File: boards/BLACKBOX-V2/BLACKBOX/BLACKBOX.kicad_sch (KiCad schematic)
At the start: 24 parts, among them J1 Micro_SD_Card, J2 Conn_01x07_Female, J3 Conn_01x02_Female, U1 Adafruit-BNO085, U2 KX122-1042, U3 MS5611-01BA

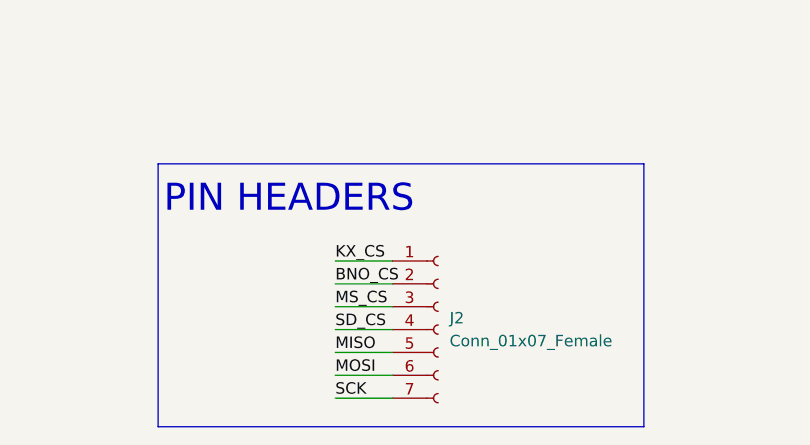
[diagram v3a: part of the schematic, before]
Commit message: Updated pcb and schematic to have 8pin headers
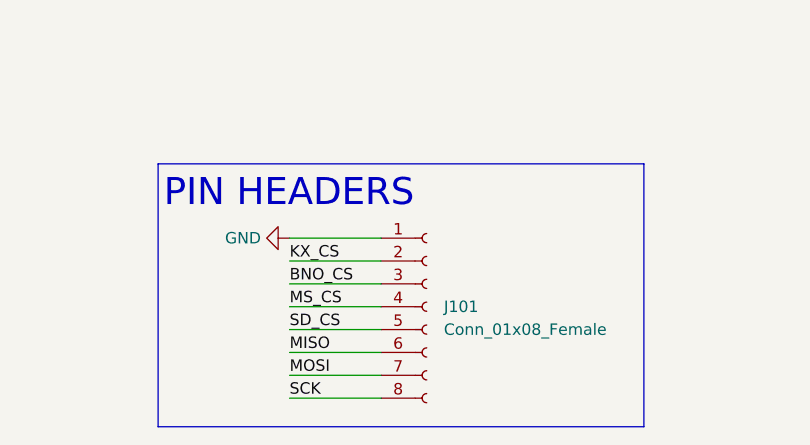
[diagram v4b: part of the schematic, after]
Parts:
- removed J2: Conn_01x07_Female, Connector_PinHeader_2.54mm:PinHeader_1x07_P2.54mm_Vertical, symbol Connector:Conn_01x07_Female
- added J101: Conn_01x08_Female, Connector_PinHeader_2.54mm:PinHeader_1x08_P2.54mm_Vertical, symbol Connector:Conn_01x08_Female
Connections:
- net BNO_CS: now also J101.3 (Pin_3)
- net GND: now also J101.1 (Pin_1)
- net KX_CS: now also J101.2 (Pin_2)
- net MISO: now also J101.6 (Pin_6)
- net MOSI: now also J101.7 (Pin_7)
- net MS_CS: now also J101.4 (Pin_4)
- net SCK: now also J101.8 (Pin_8)
- net SD_CS: now also J101.5 (Pin_5)
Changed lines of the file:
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@@
     (stroke (width 0) (type default) (color 0 0 0 0))
   )
-  (wire (pts (xy 132.715 186.69) (xy 139.065 186.69))
+  (wire (pts (xy 127.635 186.69) (xy 137.795 186.69))
     (stroke (width 0) (type default) (color 0 0 0 0))
   )
@@
     (stroke (width 0) (type default) (color 0 0 0 0))
   )
-  (wire (pts (xy 132.715 179.07) (xy 139.065 179.07))
+  (wire (pts (xy 127.635 179.07) (xy 137.795 179.07))
     (stroke (width 0) (type default) (color 0 0 0 0))
   )
@@
     (stroke (width 0) (type default) (color 0 0 0 0))
   )
-  (wire (pts (xy 132.715 173.99) (xy 139.065 173.99))
-    (stroke (width 0) (type default) (color 0 0 0 0))
-  )
-  (wire (pts (xy 132.715 184.15) (xy 139.065 184.15))
+  (wire (pts (xy 127.635 173.99) (xy 137.795 173.99))
+    (stroke (width 0) (type default) (color 0 0 0 0))
+  )
+  (wire (pts (xy 127.635 184.15) (xy 137.795 184.15))
     (stroke (width 0) (type default) (color 0 0 0 0))
   )
@@
     (stroke (width 0) (type default) (color 0 0 0 0))
   )
-  (wire (pts (xy 132.715 181.61) (xy 139.065 181.61))
+  (wire (pts (xy 127.635 181.61) (xy 137.795 181.61))
     (stroke (width 0) (type default) (color 0 0 0 0))
   )
@@
     (stroke (width 0) (type default) (color 0 0 0 0))
   )
+  (wire (pts (xy 127.635 168.91) (xy 137.795 168.91))
+    (stroke (width 0) (type default) (color 0 0 0 0))
+  )
   (wire (pts (xy 158.75 36.83) (xy 158.75 38.1))
     (stroke (width 0) (type default) (color 0 0 0 0))
@@
     (stroke (width 0) (type default) (color 0 0 0 0))
   )
-  (wire (pts (xy 132.715 176.53) (xy 139.065 176.53))
+  (wire (pts (xy 127.635 176.53) (xy 137.795 176.53))
     (stroke (width 0) (type default) (color 0 0 0 0))
   )
@@
     (stroke (width 0) (type default) (color 0 0 0 0))
   )
-  (wire (pts (xy 132.715 171.45) (xy 139.065 171.45))
+  (wire (pts (xy 127.635 171.45) (xy 137.795 171.45))
     (stroke (width 0) (type default) (color 0 0 0 0))
   )
@@
     (effects (font (size 3.2004 3.2004)) (justify left bottom))
   )
-  (text "PIN HEADERS" (at 113.665 166.37 0)
+  (text "PIN HEADERS" (at 113.665 165.735 0)
     (effects (font (size 3 3)) (justify left bottom))
   )
@@
     (effects (font (size 1.27 1.27)) (justify left bottom))
   )
-  (label "SCK" (at 132.715 186.69 0)
+  (label "SCK" (at 127.635 186.69 0)
     (effects (font (size 1.27 1.27)) (justify left bottom))
   )
@@
     (effects (font (size 1.27 1.27)) (justify left bottom))
   )
-  (label "MISO" (at 132.715 181.61 0)
+  (label "MISO" (at 127.635 181.61 0)
     (effects (font (size 1.27 1.27)) (justify left bottom))
   )
@@
     (effects (font (size 1.27 1.27)) (justify left bottom))
   )
-  (label "MS_CS" (at 132.715 176.53 0)
+  (label "MS_CS" (at 127.635 176.53 0)
     (effects (font (size 1.27 1.27)) (justify left bottom))
   )
@@
     (effects (font (size 1.27 1.27)) (justify left bottom))
   )
-  (label "KX_CS" (at 132.715 171.45 0)
+  (label "KX_CS" (at 127.635 171.45 0)
     (effects (font (size 1.27 1.27)) (justify left bottom))
   )
@@
     (effects (font (size 1.27 1.27)) (justify left bottom))
   )
-  (label "MOSI" (at 132.715 184.15 0)
+  (label "MOSI" (at 127.635 184.15 0)
     (effects (font (size 1.27 1.27)) (justify left bottom))
   )
@@
     (effects (font (size 1.27 1.27)) (justify left bottom))
   )
-  (label "SD_CS" (at 132.715 179.07 0)
+  (label "SD_CS" (at 127.635 179.07 0)
     (effects (font (size 1.27 1.27)) (justify left bottom))
   )
@@
     (effects (font (size 1.27 1.27)) (justify left bottom))
   )
-  (label "BNO_CS" (at 132.715 173.99 0)
+  (label "BNO_CS" (at 127.635 173.99 0)
     (effects (font (size 1.27 1.27)) (justify left bottom))
   )
@@
     (pin "2")
   )
-  (symbol (lib_id "Connector:Conn_01x07_Female") (at 144.145 179.07 0) (unit 1)
-    (in_bom yes) (on_board yes) (fields_autoplaced)
-    (property "Reference" "J2" (id 0) (at 145.415 177.7999 0)
-      (effects (font (size 1.27 1.27)) (justify left))
-    )
-    (property "Value" "Conn_01x07_Female" (id 1) (at 145.415 180.3399 0)
-      (effects (font (size 1.27 1.27)) (justify left))
-    )
-    (property "Footprint" "Connector_PinHeader_2.54mm:PinHeader_1x07_P2.54mm_Vertical" (id 2) (at 144.145 179.07 0)
-      (effects (font (size 1.27 1.27)) hide)
-    )
-    (property "Datasheet" "~" (id 3) (at 144.145 179.07 0)
-      (effects (font (size 1.27 1.27)) hide)
-    )
-    (pin "1")
-    (pin "2")
-    (pin "3")
-    (pin "4")
-    (pin "5")
-    (pin "6")
-    (pin "7")
-  )
   (symbol (lib_id "Device:C_Small") (at 78.74 26.035 90) (unit 1)
     (in_bom yes) (on_board yes) (fields_autoplaced)
@@
     (pin "1")
   )
+  (symbol (lib_id "Connector:Conn_01x08_Female") (at 142.875 176.53 0) (unit 1)
+    (in_bom yes) (on_board yes) (fields_autoplaced)
+    (property "Reference" "J101" (id 0) (at 144.78 176.5299 0)
+      (effects (font (size 1.27 1.27)) (justify left))
+    )
+    (property "Value" "Conn_01x08_Female" (id 1) (at 144.78 179.0699 0)
+      (effects (font (size 1.27 1.27)) (justify left))
+    )
+    (property "Footprint" "Connector_PinHeader_2.54mm:PinHeader_1x08_P2.54mm_Vertical" (id 2) (at 142.875 176.53 0)
+      (effects (font (size 1.27 1.27)) hide)
+    )
+    (property "Datasheet" "~" (id 3) (at 142.875 176.53 0)
+      (effects (font (size 1.27 1.27)) hide)
+    )
+    (pin "1")
+    (pin "2")
+    (pin "3")
+    (pin "4")
+    (pin "5")
+    (pin "6")
+    (pin "7")
+    (pin "8")
+  )
+  (symbol (lib_id "power:GND") (at 127.635 168.91 270) (unit 1)
+    (in_bom yes) (on_board yes)
+    (property "Reference" "#PWR0101" (id 0) (at 121.285 168.91 0)
+      (effects (font (size 1.27 1.27)) hide)
+    )
+    (property "Value" "GND" (id 1) (at 124.46 168.9099 90)
+      (effects (font (size 1.27 1.27)) (justify right))
+    )
+    (property "Footprint" "" (id 2) (at 127.635 168.91 0)
+      (effects (font (size 1.27 1.27)) hide)
+    )
+    (property "Datasheet" "" (id 3) (at 127.635 168.91 0)
+      (effects (font (size 1.27 1.27)) hide)
+    )
+    (pin "1")
+  )
   (symbol (lib_id "Device:Jumper_NC_Small") (at 252.222 33.274 0) (unit 1)
     (in_bom yes) (on_board yes)
@@
       (reference "#PWR018") (unit 1) (value "GND") (footprint "")
     )
+    (path "/9a261a05-f51b-41db-af95-8182bda7df0f"
+      (reference "#PWR0101") (unit 1) (value "GND") (footprint "")
+    )
     (path "/04c2f4a0-ab0f-4d7a-91c1-dde2ab8ebf89"
       (reference "A1") (unit 1) (value "Arduino_Nano_v3.x") (footprint "Module:Arduino_Nano")
@@
       (reference "J1") (unit 1) (value "Micro_SD_Card") (footprint "Connector_Card:microSD_HC_Hirose_DM3AT-SF-PEJM5")
     )
-    (path "/28be4453-0358-472e-94e9-5e8d78d2b655"
-      (reference "J2") (unit 1) (value "Conn_01x07_Female") (footprint "Connector_PinHeader_2.54mm:PinHeader_1x07_P2.54mm_Vertical")
-    )
     (path "/eaf8df72-2293-43bc-a95d-5a36de237e99"
       (reference "J3") (unit 1) (value "Conn_01x02_Female") (footprint "Connector_JST:JST_PH_B2B-PH-K_1x02_P2.00mm_Vertical")
     )
+    (path "/8c1aa14f-b92e-48a9-8685-2f98cff5b3f9"
+      (reference "J101") (unit 1) (value "Conn_01x08_Female") (footprint "Connector_PinHeader_2.54mm:PinHeader_1x08_P2.54mm_Vertical")
+    )
     (path "/30afc378-2f36-4761-a0c7-cd6bc7d246e3"

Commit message: Completed power thingy
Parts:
- added J102: Conn_01x02_Female, Connector_JST:JST_PH_B2B-PH-K_1x02_P2.00mm_Vertical, symbol Connector:Conn_01x02_Female
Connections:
- net GND: now also J102.1 (Pin_1); no longer J3.1 (Pin_1)
- new net VBUS: J102.2 (Pin_2), J3.1 (Pin_1)
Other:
- moved on the sheet: J3
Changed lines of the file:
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@@
     (stroke (width 0) (type default) (color 0 0 0 0))
   )
-  (polyline (pts (xy 279.4 96.52) (xy 279.4 72.39))
+  (polyline (pts (xy 279.4 104.775) (xy 279.4 72.39))
     (stroke (width 0) (type default) (color 0 0 0 0))
   )
@@
     (stroke (width 0) (type default) (color 0 0 0 0))
   )
-  (wire (pts (xy 242.57 83.82) (xy 240.03 83.82))
+  (wire (pts (xy 230.505 81.915) (xy 227.965 81.915))
     (stroke (width 0) (type default) (color 0 0 0 0))
   )
@@
     (stroke (width 0) (type default) (color 0 0 0 0))
   )
-  (polyline (pts (xy 220.98 96.52) (xy 279.4 96.52))
+  (polyline (pts (xy 220.98 104.775) (xy 279.4 104.775))
     (stroke (width 0) (type default) (color 0 0 0 0))
   )
@@
     (stroke (width 0) (type default) (color 0 0 0 0))
   )
-  (wire (pts (xy 240.03 83.82) (xy 240.03 88.9))
+  (wire (pts (xy 227.965 81.915) (xy 227.965 86.995))
     (stroke (width 0) (type default) (color 0 0 0 0))
   )
@@
     (stroke (width 0) (type default) (color 0 0 0 0))
   )
-  (wire (pts (xy 242.57 81.28) (xy 236.22 81.28))
+  (wire (pts (xy 230.505 79.375) (xy 224.155 79.375))
     (stroke (width 0) (type default) (color 0 0 0 0))
   )
@@
     (stroke (width 0) (type default) (color 0 0 0 0))
   )
-  (polyline (pts (xy 219.71 72.39) (xy 219.71 96.52))
+  (polyline (pts (xy 219.71 72.39) (xy 219.71 104.775))
     (stroke (width 0) (type default) (color 0 0 0 0))
   )
@@
     (stroke (width 0) (type default) (color 0 0 0 0))
   )
+  (wire (pts (xy 247.65 87.63) (xy 241.3 87.63))
+    (stroke (width 0) (type default) (color 0 0 0 0))
+  )
+  (wire (pts (xy 245.11 90.17) (xy 245.11 95.25))
+    (stroke (width 0) (type default) (color 0 0 0 0))
+  )
   (wire (pts (xy 153.67 88.9) (xy 153.67 90.17))
     (stroke (width 0) (type default) (color 0 0 0 0))
@@
     (stroke (width 0) (type default) (color 0 0 0 0))
   )
+  (wire (pts (xy 247.65 90.17) (xy 245.11 90.17))
+    (stroke (width 0) (type default) (color 0 0 0 0))
+  )
   (wire (pts (xy 47.625 50.8) (xy 57.785 50.8))
     (stroke (width 0) (type default) (color 0 0 0 0))
@@
     (stroke (width 0) (type default) (color 0 0 0 0))
   )
+  (wire (pts (xy 241.3 87.63) (xy 241.3 95.25))
+    (stroke (width 0) (type default) (color 0 0 0 0))
+  )
   (wire (pts (xy 242.316 52.705) (xy 251.079 52.705))
     (stroke (width 0) (type default) (color 0 0 0 0))
@@
     (stroke (width 0) (type default) (color 0 0 0 0))
   )
-  (wire (pts (xy 236.22 81.28) (xy 236.22 88.9))
+  (wire (pts (xy 224.155 79.375) (xy 224.155 86.995))
     (stroke (width 0) (type default) (color 0 0 0 0))
   )
@@
   )
   (wire (pts (xy 48.26 111.76) (xy 53.34 111.76))
-    (stroke (width 0) (type default) (color 0 0 0 0))
-  )
-  (polyline (pts (xy 219.71 96.52) (xy 226.06 96.52))
     (stroke (width 0) (type default) (color 0 0 0 0))
   )
@@
     (effects (font (size 1.27 1.27)) (justify left bottom))
   )
-  (symbol (lib_id "power:VCC") (at 240.03 88.9 180) (unit 1)
-    (in_bom yes) (on_board yes) (fields_autoplaced)
-    (property "Reference" "#PWR015" (id 0) (at 240.03 85.09 0)
-      (effects (font (size 1.27 1.27)) hide)
-    )
-    (property "Value" "VCC" (id 1) (at 240.03 93.98 0))
-    (property "Footprint" "" (id 2) (at 240.03 88.9 0)
-      (effects (font (size 1.27 1.27)) hide)
-    )
-    (property "Datasheet" "" (id 3) (at 240.03 88.9 0)
+  (symbol (lib_id "power:VCC") (at 227.965 86.995 180) (unit 1)
+    (in_bom yes) (on_board yes) (fields_autoplaced)
+    (property "Reference" "#PWR015" (id 0) (at 227.965 83.185 0)
+      (effects (font (size 1.27 1.27)) hide)
+    )
+    (property "Value" "VCC" (id 1) (at 227.965 92.075 0))
+    (property "Footprint" "" (id 2) (at 227.965 86.995 0)
+      (effects (font (size 1.27 1.27)) hide)
+    )
+    (property "Datasheet" "" (id 3) (at 227.965 86.995 0)
       (effects (font (size 1.27 1.27)) hide)
     )
@@
     (pin "2")
   )
+  (symbol (lib_id "power:VBUS") (at 224.155 86.995 180) (unit 1)
+    (in_bom yes) (on_board yes) (fields_autoplaced)
+    (property "Reference" "#PWR0102" (id 0) (at 224.155 83.185 0)
+      (effects (font (size 1.27 1.27)) hide)
+    )
+    (property "Value" "VBUS" (id 1) (at 224.155 92.075 0))
+    (property "Footprint" "" (id 2) (at 224.155 86.995 0)
+      (effects (font (size 1.27 1.27)) hide)
+    )
+    (property "Datasheet" "" (id 3) (at 224.155 86.995 0)
+      (effects (font (size 1.27 1.27)) hide)
+    )
+    (pin "1")
+  )
+  (symbol (lib_id "Connector:Conn_01x02_Female") (at 252.73 87.63 0) (unit 1)
+    (in_bom yes) (on_board yes) (fields_autoplaced)
+    (property "Reference" "J102" (id 0) (at 254 87.6299 0)
+      (effects (font (size 1.27 1.27)) (justify left))
+    )
+    (property "Value" "Conn_01x02_Female" (id 1) (at 254 90.1699 0)
+      (effects (font (size 1.27 1.27)) (justify left))
+    )
+    (property "Footprint" "Connector_JST:JST_PH_B2B-PH-K_1x02_P2.00mm_Vertical" (id 2) (at 252.73 87.63 0)
+      (effects (font (size 1.27 1.27)) hide)
+    )
+    (property "Datasheet" "~" (id 3) (at 252.73 87.63 0)
+      (effects (font (size 1.27 1.27)) hide)
+    )
+    (pin "1")
+    (pin "2")
+  )
   (symbol (lib_id "Device:LED") (at 245.745 131.445 180) (unit 1)
     (in_bom yes) (on_board yes)
@@
     (pin "1")
     (pin "2")
+  )
+  (symbol (lib_id "power:VBUS") (at 245.11 95.25 180) (unit 1)
+    (in_bom yes) (on_board yes) (fields_autoplaced)
+    (property "Reference" "#PWR0104" (id 0) (at 245.11 91.44 0)
+      (effects (font (size 1.27 1.27)) hide)
+    )
+    (property "Value" "VBUS" (id 1) (at 245.11 100.33 0))
+    (property "Footprint" "" (id 2) (at 245.11 95.25 0)
+      (effects (font (size 1.27 1.27)) hide)
+    )
+    (property "Datasheet" "" (id 3) (at 245.11 95.25 0)
+      (effects (font (size 1.27 1.27)) hide)
+    )
+    (pin "1")
   )
   (symbol (lib_id "Device:Jumper_NC_Small") (at 57.785 32.385 0) (unit 1)
@@
     (pin "1")
   )
-  (symbol (lib_id "power:GND") (at 236.22 88.9 0) (unit 1)
-    (in_bom yes) (on_board yes) (fields_autoplaced)
-    (property "Reference" "#PWR014" (id 0) (at 236.22 95.25 0)
-      (effects (font (size 1.27 1.27)) hide)
-    )
-    (property "Value" "GND" (id 1) (at 236.22 93.98 0))
-    (property "Footprint" "" (id 2) (at 236.22 88.9 0)
-      (effects (font (size 1.27 1.27)) hide)
-    )
-    (property "Datasheet" "" (id 3) (at 236.22 88.9 0)
-      (effects (font (size 1.27 1.27)) hide)
-    )
-    (pin "1")
-  )
   (symbol (lib_id "power:GND") (at 67.945 64.77 0) (unit 1)
     (in_bom yes) (on_board yes) (fields_autoplaced)
@@
     (pin "8")
   )
+  (symbol (lib_id "power:GND") (at 241.3 95.25 0) (unit 1)
+    (in_bom yes) (on_board yes) (fields_autoplaced)
+    (property "Reference" "#PWR0103" (id 0) (at 241.3 101.6 0)
+      (effects (font (size 1.27 1.27)) hide)
+    )
+    (property "Value" "GND" (id 1) (at 241.3 100.33 0))
+    (property "Footprint" "" (id 2) (at 241.3 95.25 0)
+      (effects (font (size 1.27 1.27)) hide)
+    )
+    (property "Datasheet" "" (id 3) (at 241.3 95.25 0)
+      (effects (font (size 1.27 1.27)) hide)
+    )
+    (pin "1")
+  )
   (symbol (lib_id "power:GND") (at 127.635 168.91 270) (unit 1)
     (in_bom yes) (on_board yes)
@@
     (pin "2")
   )
-  (symbol (lib_id "Connector:Conn_01x02_Female") (at 247.65 81.28 0) (unit 1)
-    (in_bom yes) (on_board yes) (fields_autoplaced)
-    (property "Reference" "J3" (id 0) (at 248.92 81.2799 0)
-      (effects (font (size 1.27 1.27)) (justify left))
-    )
-    (property "Value" "Conn_01x02_Female" (id 1) (at 248.92 83.8199 0)
-      (effects (font (size 1.27 1.27)) (justify left))
-    )
-    (property "Footprint" "Connector_JST:JST_PH_B2B-PH-K_1x02_P2.00mm_Vertical" (id 2) (at 247.65 81.28 0)
-      (effects (font (size 1.27 1.27)) hide)
-    )
-    (property "Datasheet" "~" (id 3) (at 247.65 81.28 0)
+  (symbol (lib_id "Connector:Conn_01x02_Female") (at 235.585 79.375 0) (unit 1)
+    (in_bom yes) (on_board yes) (fields_autoplaced)
+    (property "Reference" "J3" (id 0) (at 236.855 79.3749 0)
+      (effects (font (size 1.27 1.27)) (justify left))
+    )
+    (property "Value" "Conn_01x02_Female" (id 1) (at 236.855 81.9149 0)
+      (effects (font (size 1.27 1.27)) (justify left))
+    )
+    (property "Footprint" "Connector_JST:JST_PH_B2B-PH-K_1x02_P2.00mm_Vertical" (id 2) (at 235.585 79.375 0)
+      (effects (font (size 1.27 1.27)) hide)
+    )
+    (property "Datasheet" "~" (id 3) (at 235.585 79.375 0)
       (effects (font (size 1.27 1.27)) hide)
     )
@@
       (reference "#PWR013") (unit 1) (value "+5V") (footprint "")
     )
-    (path "/71a8a660-9742-4f65-9d97-408dcbaa9dfa"
-      (reference "#PWR014") (unit 1) (value "GND") (footprint "")
-    )
     (path "/049eb2fb-4622-4f7a-a922-102260eb053c"
       (reference "#PWR015") (unit 1) (value "VCC") (footprint "")
@@
       (reference "#PWR0101") (unit 1) (value "GND") (footprint "")
     )
+    (path "/1736f033-6f2a-4216-b38c-b493599dea54"
+      (reference "#PWR0102") (unit 1) (value "VBUS") (footprint "")
+    )
+    (path "/91918576-90a2-49b7-93e3-469853563e5c"
+      (reference "#PWR0103") (unit 1) (value "GND") (footprint "")
+    )
+    (path "/2e239411-486c-4ae6-944a-17a804ae2fc3"
+      (reference "#PWR0104") (unit 1) (value "VBUS") (footprint "")
+    )
     (path "/04c2f4a0-ab0f-4d7a-91c1-dde2ab8ebf89"
       (reference "A1") (unit 1) (value "Arduino_Nano_v3.x") (footprint "Module:Arduino_Nano")
@@
       (reference "J101") (unit 1) (value "Conn_01x08_Female") (footprint "Connector_PinHeader_2.54mm:PinHeader_1x08_P2.54mm_Vertical")
     )
+    (path "/17776c7f-f0d1-4b23-8c32-65e30a5f3c43"
+      (reference "J102") (unit 1) (value "Conn_01x02_Female") (footprint "Connector_JST:JST_PH_B2B-PH-K_1x02_P2.00mm_Vertical")
+    )
     (path "/30afc378-2f36-4761-a0c7-cd6bc7d246e3"
